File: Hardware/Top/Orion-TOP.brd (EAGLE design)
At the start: 38 x 38 mm, 49 parts, among them U2 NRF52832_MODULE_MDBT42, U5 PCF8523

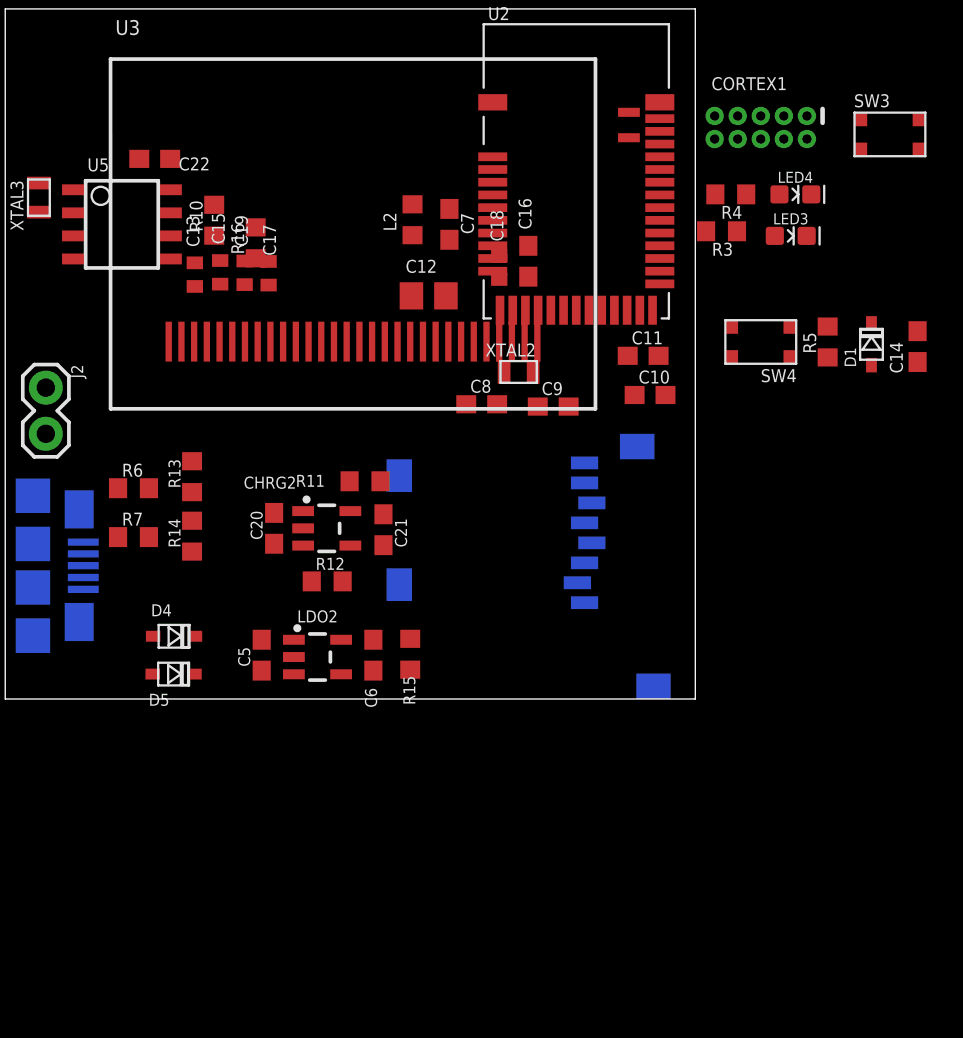
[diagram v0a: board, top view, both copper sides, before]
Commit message: modified top board schemetics: add buttons and organized
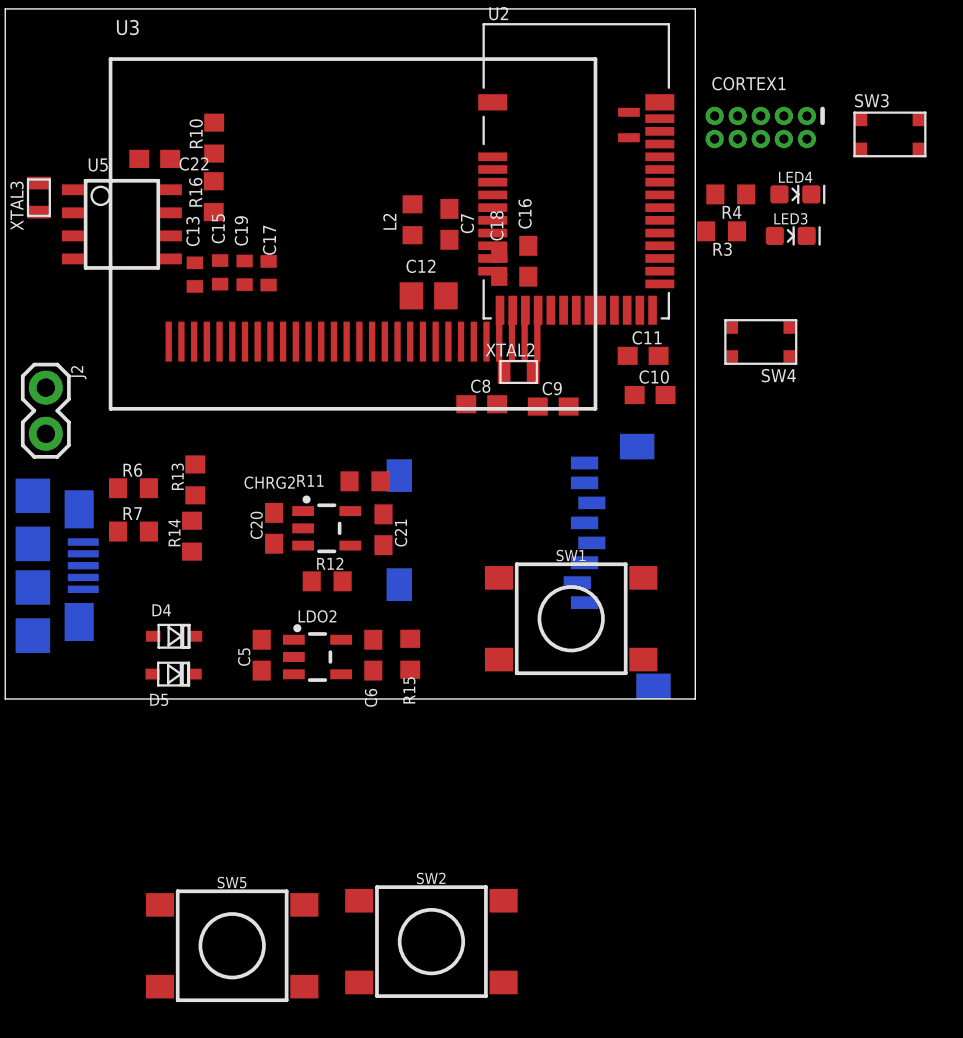
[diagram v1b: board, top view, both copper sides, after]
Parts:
- removed C14: 100n, LinnesLab-Passives:C0603
- removed D1: (no value), LinnesLab-DiscreteSemi:USC
- removed R5: 10k, LinnesLab-Passives:R0603
- added SW1, SW2, SW5: SWITCH.MOM, LinnesLab-Switches:TACTILE_SWITCH_SMD_6.2MM_TALL
- moved R10 4.52 mm to (11.5, 30.9)
- moved R16 3.43 mm to (11.5, 27.7)
- moved R7 0.30 mm to (7.06, 9.22)
- moved R13 0.25 mm to (10.5, 12.1)
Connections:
- removed net DTR: C14.1
- new net SW1: SW1.A1, SW2.A1, SW5.A1
- net 3.3V: no longer D1.-, R5.2
- net GND: now also SW1.B1, SW1.B2, SW2.B1, SW2.B2, SW5.B1, SW5.B2
- net RESET: no longer C14.2, D1.+, R5.1

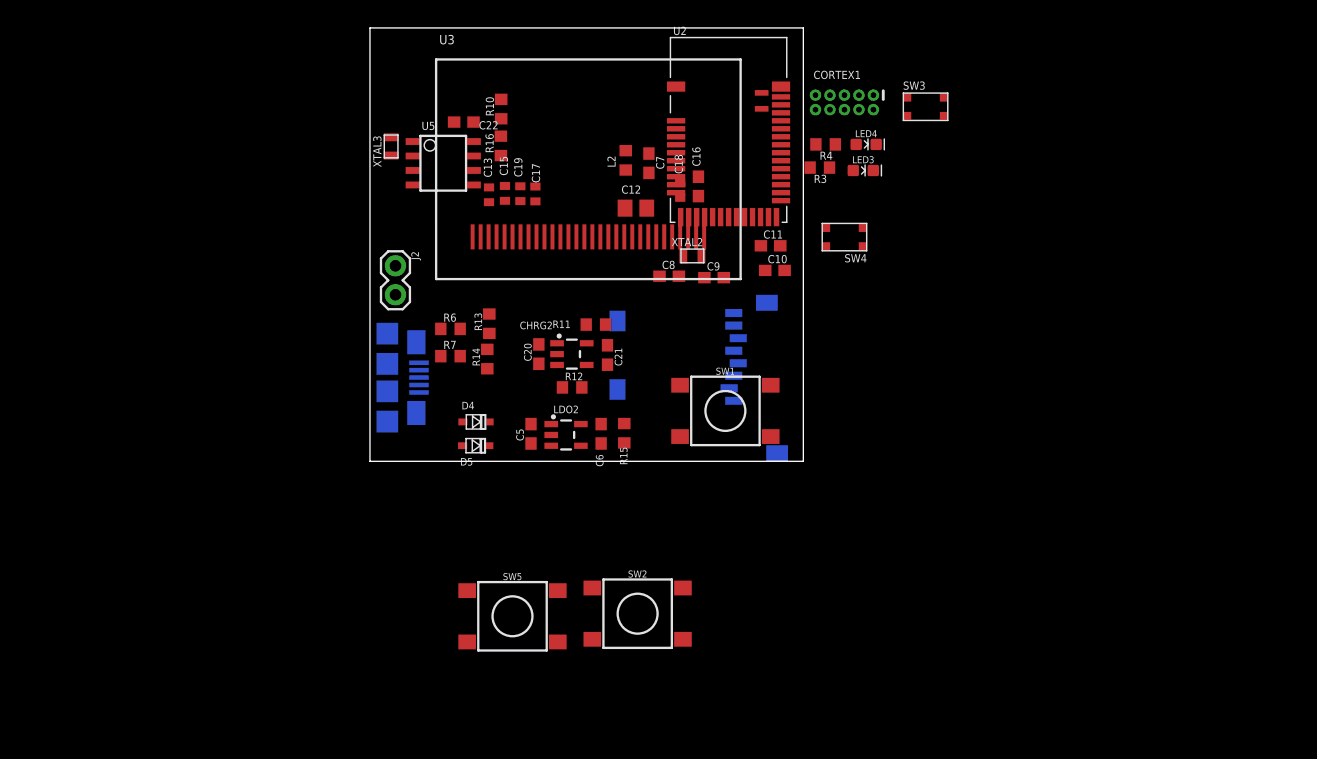
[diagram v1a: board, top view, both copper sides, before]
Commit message: fixed some missing design blocks
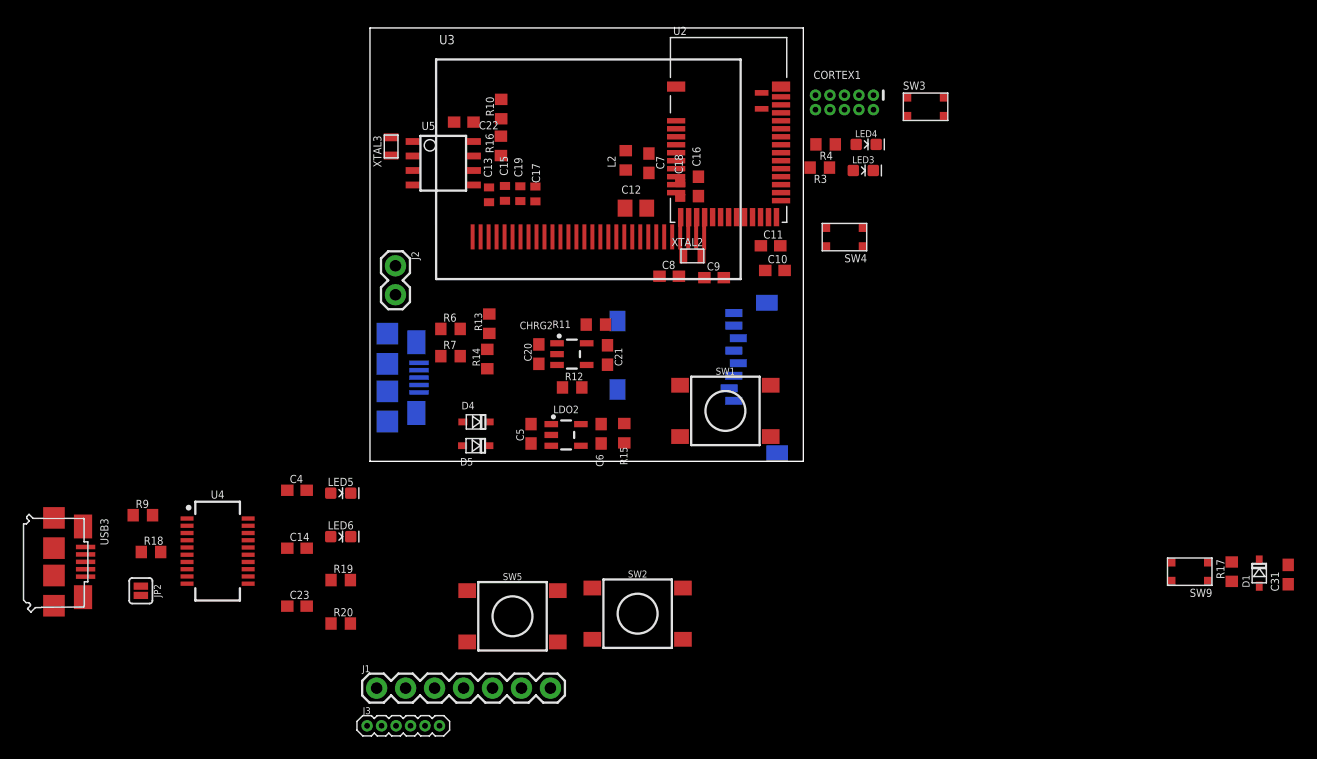
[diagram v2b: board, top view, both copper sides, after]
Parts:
- added C14, C23: 47p, LinnesLab-Passives:C0603
- added C31, C4: 100n, LinnesLab-Passives:C0603
- added D1: (no value), LinnesLab-DiscreteSemi:USC
- added J1: (no value), LinnesLab-Connectors:1X07
- added J3: (no value), LinnesLab-Connectors:1X06_1.27MM
- added JP2: (no value), LinnesLab-Switches:SMT-JUMPER_2_NO_SILK
- added LED5: RED, LinnesLab-LED:LED-0603
- added LED6: YELLOW, LinnesLab-LED:LED-0603
- added R17: 10k, LinnesLab-Passives:R0603
- added R18, R9: 27, LinnesLab-Passives:R0603
- added R19, R20: 1k, LinnesLab-Passives:R0603
- added SW9: (no value), LinnesLab-Switches:BUTTON-GULLWING
- added U4: FT231XS, LinnesLab-DigitalIC:SSOP20_L
- added USB3: USB.MICRO-BIGGERPADS, LinnesLab-Connectors:USB-MICRO-01.BIGGERPADS
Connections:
- removed net BATT: R13.1, R14.2
- removed net CHRG.STAT: CHRG2.1, R12.1
- removed net SD.CS: SD2.2
- new net !CTS: JP2.2, U4.9
- new net !DTR: U4.1
- new net A4/BATT: R13.1, R14.2, U2.5
- new net D11/SW1: SW1.A1, U2.25
- new net D15/SW2: SW2.A1, U2.29
- new net D27/CHRG.STATUS: CHRG2.1, R12.1, U2.4
- new net D7/SD.CS: SD2.2, U2.20
- new net DTR: C31.1
- new net FT3V3: U4.13
- new net N$23: R9.2, U4.12
- new net N$24: R18.2, U4.11
- new net N$25: LED5.C, R19.2
- new net N$26: LED6.C, R20.2
- new net RXLED: R19.1, U4.17
- new net TXLED: R20.1, U4.10
- new net USB_D+: C14.1, R18.1, USB3.3
- new net USB_D-: C23.2, R9.1, USB3.2
- net 3.3V: now also C4.2, D1.-, LED5.A, LED6.A, R17.2, U4.14, U4.3
- net GND: now also C14.2, C23.1, C4.1, JP2.1, SW9.3, U4.16, U4.6, USB3.5, USB3.S1, USB3.S2, USB3.S3, USB3.S4, USB3.S5, USB3.S6
- net RESET: now also C31.2, D1.+, R17.1, SW9.1
- net RXD: now also U4.4
- net SW1: no longer SW1.A1, SW2.A1
- net TXD: now also U4.20
- net V_USB: now also U4.15, USB3.1
